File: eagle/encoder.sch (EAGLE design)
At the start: 29 parts, among them IC1 LM339D, J1 SPI, U1 MCP42XXX, U2 ATMEGA328P

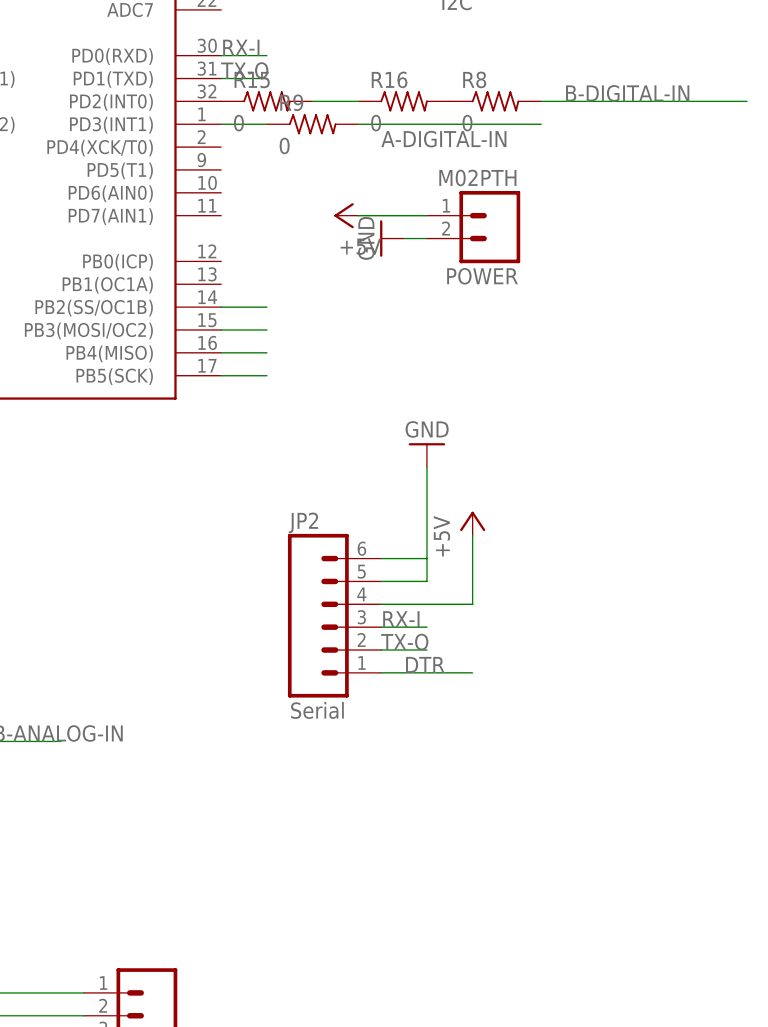
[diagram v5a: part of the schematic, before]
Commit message: Added LED indicator.
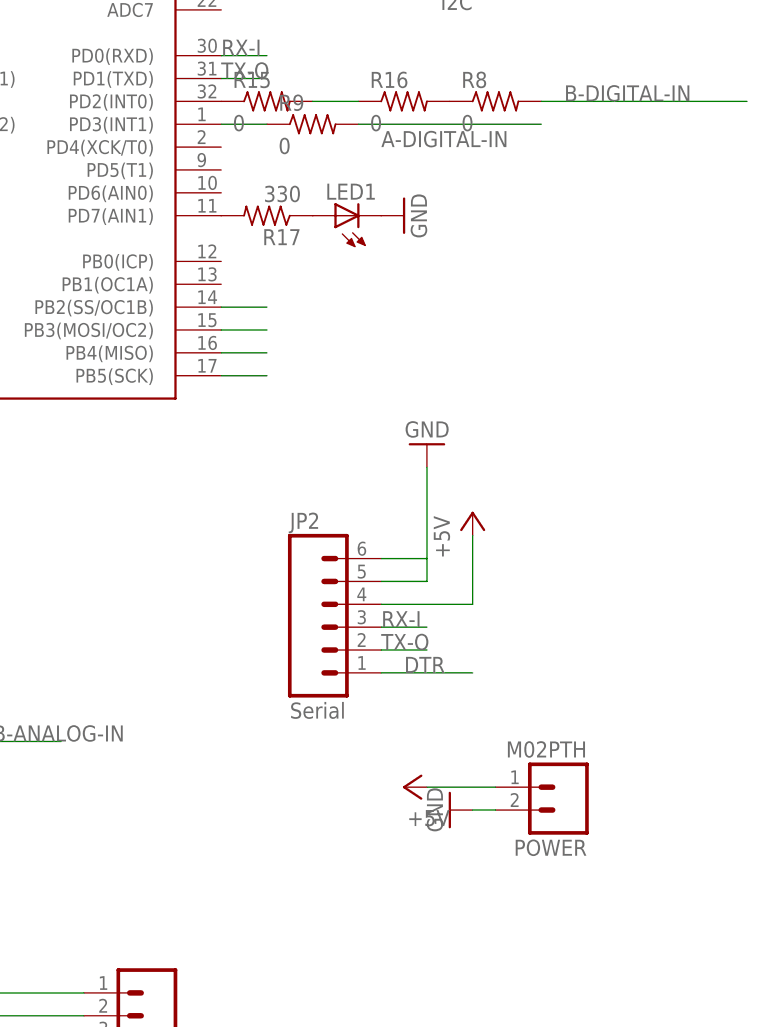
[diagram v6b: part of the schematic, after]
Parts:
- added LED1: (no value), led:LEDSMT1206
- added R17: 330, resistor:R-US_R1206
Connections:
- new net N$16: LED1.A, R17.1
- new net N$17: R17.2, U2.PD7(AIN1)
- net GND: now also LED1.C
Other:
- moved on the sheet: POWER
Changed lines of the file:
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@@
 <part name="R15" library="resistor" deviceset="R-US_" device="R1206" value="0"/>
 <part name="R16" library="resistor" deviceset="R-US_" device="R1206" value="0"/>
+<part name="LED1" library="led" deviceset="LED" device="SMT1206"/>
+<part name="R17" library="resistor" deviceset="R-US_" device="R1206" value="330"/>
+<part name="GND13" library="supply1" deviceset="GND" device=""/>
 </parts>
 <sheets>
@@
 <instance part="P+13" gate="1" x="124.46" y="137.16"/>
 <instance part="I2C" gate="G$1" x="121.92" y="200.66" rot="R180"/>
-<instance part="POWER" gate="G$1" x="127" y="170.18" rot="R180"/>
-<instance part="P+14" gate="1" x="109.22" y="170.18" rot="R90"/>
-<instance part="GND12" gate="1" x="114.3" y="167.64" rot="R270"/>
+<instance part="POWER" gate="G$1" x="134.62" y="106.68" rot="R180"/>
+<instance part="P+14" gate="1" x="116.84" y="106.68" rot="R90"/>
+<instance part="GND12" gate="1" x="121.92" y="104.14" rot="R270"/>
 <instance part="R15" gate="G$1" x="101.6" y="182.88"/>
 <instance part="R16" gate="G$1" x="116.84" y="182.88"/>
+<instance part="LED1" gate="G$1" x="109.22" y="170.18" rot="R90"/>
+<instance part="R17" gate="G$1" x="101.6" y="170.18" rot="R180"/>
+<instance part="GND13" gate="1" x="116.84" y="170.18" rot="R90"/>
 </instances>
 <busses>
@@
 <pinref part="POWER" gate="G$1" pin="1"/>
 <pinref part="P+14" gate="1" pin="+5V"/>
-<wire x1="111.76" y1="170.18" x2="119.38" y2="170.18" width="0.1524" layer="91"/>
+<wire x1="119.38" y1="106.68" x2="127" y2="106.68" width="0.1524" layer="91"/>
 </segment>
 </net>
@@
 <pinref part="POWER" gate="G$1" pin="2"/>
 <pinref part="GND12" gate="1" pin="GND"/>
-<wire x1="119.38" y1="167.64" x2="116.84" y2="167.64" width="0.1524" layer="91"/>
+<wire x1="127" y1="104.14" x2="124.46" y2="104.14" width="0.1524" layer="91"/>
+</segment>
+<segment>
+<pinref part="LED1" gate="G$1" pin="C"/>
+<pinref part="GND13" gate="1" pin="GND"/>
 </segment>
 </net>
@@
 </segment>
 </net>
+<net name="N$16" class="0">
+<segment>
+<pinref part="LED1" gate="G$1" pin="A"/>
+<pinref part="R17" gate="G$1" pin="1"/>
+</segment>
+</net>
+<net name="N$17" class="0">
+<segment>
+<pinref part="U2" gate="G$1" pin="PD7(AIN1)"/>
+<pinref part="R17" gate="G$1" pin="2"/>
+</segment>
+</net>

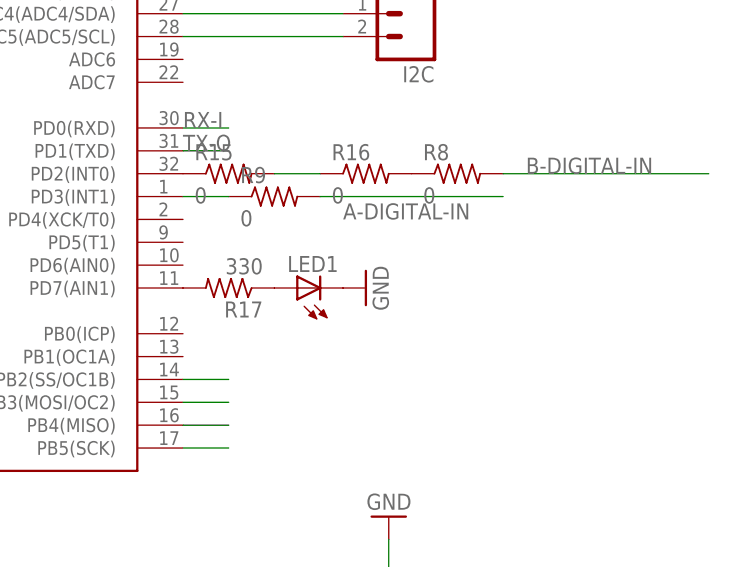
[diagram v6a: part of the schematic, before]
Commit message: Thinned some traces to provide sufficient clearance.
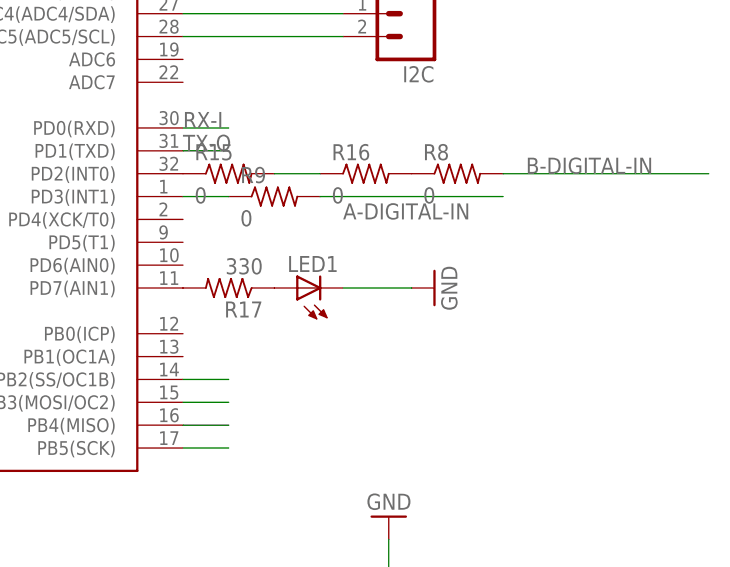
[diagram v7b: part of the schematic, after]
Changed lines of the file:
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@@
 </variantdefs>
 <classes>
-<class number="0" name="default" width="0" drill="0">
+<class number="0" name="default" width="0.254" drill="0">
+<clearance class="0" value="0.2032"/>
 </class>
 </classes>
@@
 <instance part="LED1" gate="G$1" x="109.22" y="170.18" rot="R90"/>
 <instance part="R17" gate="G$1" x="101.6" y="170.18" rot="R180"/>
-<instance part="GND13" gate="1" x="116.84" y="170.18" rot="R90"/>
+<instance part="GND13" gate="1" x="124.46" y="170.18" rot="R90"/>
 </instances>
 <busses>
@@
 <pinref part="LED1" gate="G$1" pin="C"/>
 <pinref part="GND13" gate="1" pin="GND"/>
+<wire x1="121.92" y1="170.18" x2="114.3" y2="170.18" width="0.1524" layer="91"/>
 </segment>
 </net>

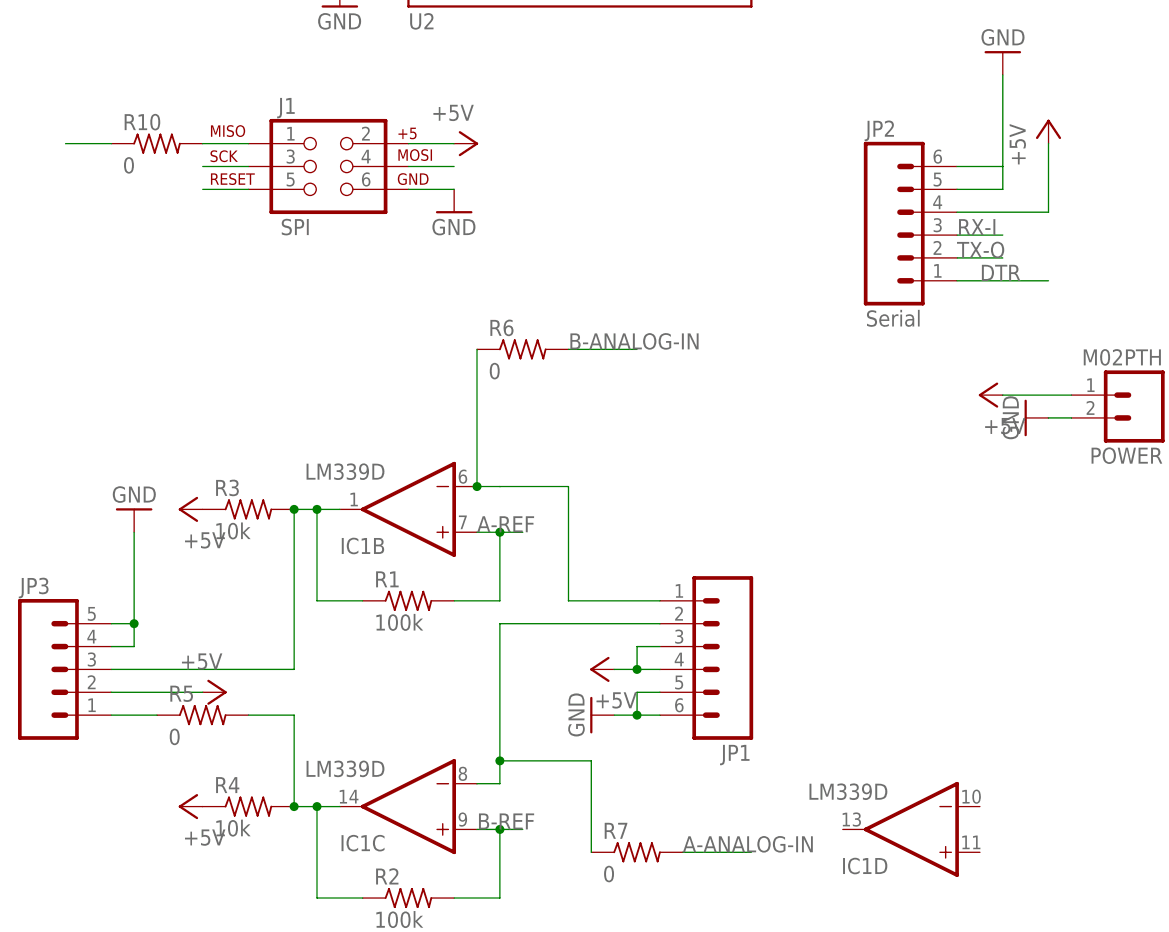
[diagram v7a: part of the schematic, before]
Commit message: Made corners 45 degrees as opposed to 90.
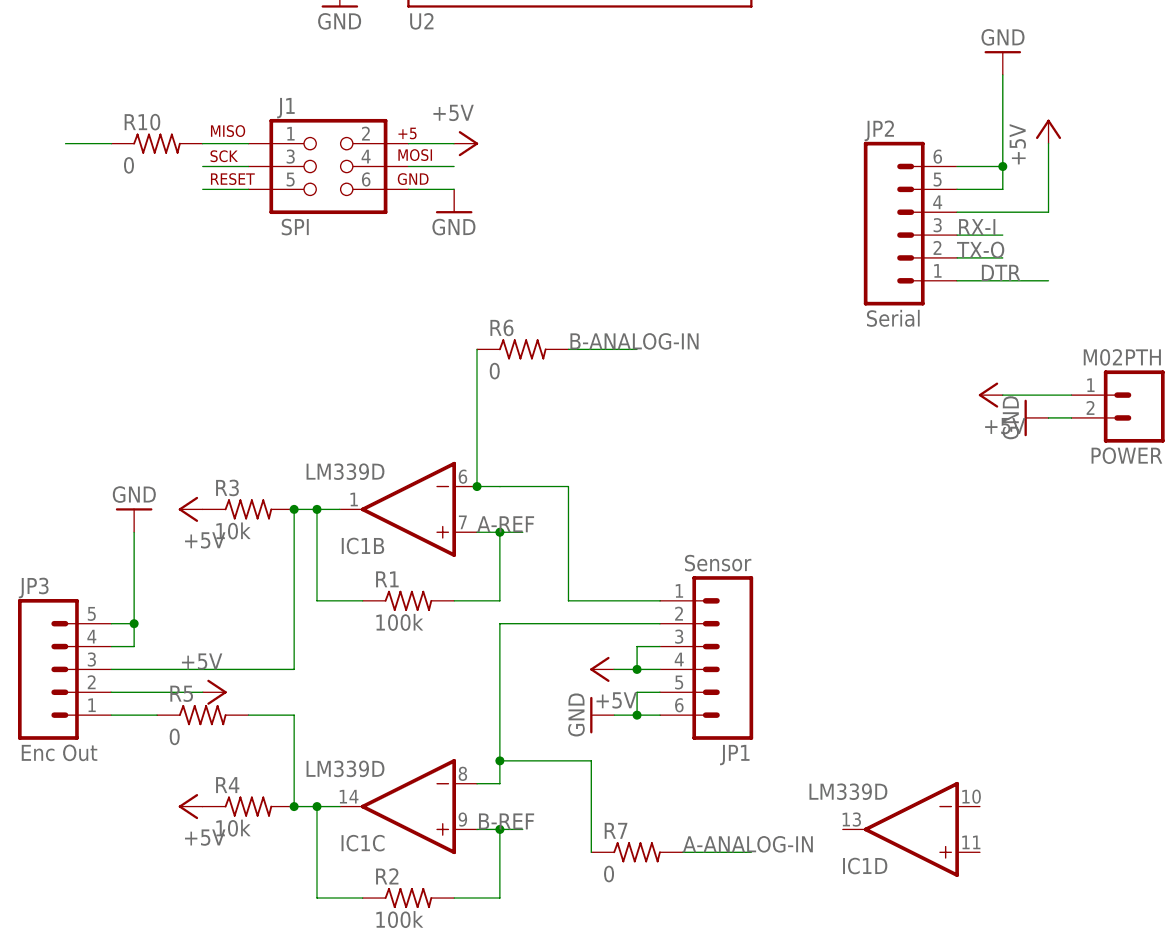
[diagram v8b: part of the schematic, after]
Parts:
- JP1: value (none) -> Sensor
- JP3: value (none) -> Enc Out
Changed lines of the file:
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@@
 <part name="GND3" library="supply1" deviceset="GND" device=""/>
 <part name="GND4" library="supply1" deviceset="GND" device=""/>
-<part name="JP1" library="SparkFun-Connectors" deviceset="M06" device="SIP"/>
+<part name="JP1" library="SparkFun-Connectors" deviceset="M06" device="SIP" value="Sensor"/>
 <part name="P+5" library="supply1" deviceset="+5V" device=""/>
 <part name="GND5" library="supply1" deviceset="GND" device=""/>
 <part name="P+6" library="supply1" deviceset="+5V" device=""/>
 <part name="P+7" library="supply1" deviceset="+5V" device=""/>
-<part name="JP3" library="SparkFun-Connectors" deviceset="M05" device="NO_SILK"/>
+<part name="JP3" library="SparkFun-Connectors" deviceset="M05" device="NO_SILK" value="Enc Out"/>
 <part name="GND7" library="supply1" deviceset="GND" device=""/>
 <part name="P+8" library="supply1" deviceset="+5V" device=""/>
@@
 <wire x1="114.3" y1="132.08" x2="119.38" y2="132.08" width="0.1524" layer="91"/>
 <pinref part="GND11" gate="1" pin="GND"/>
-</segment>
-<segment>
+<junction x="119.38" y="132.08"/>
+</segment>
+<segment>
